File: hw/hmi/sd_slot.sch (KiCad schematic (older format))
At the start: 10 parts, among them J7 SD_Card

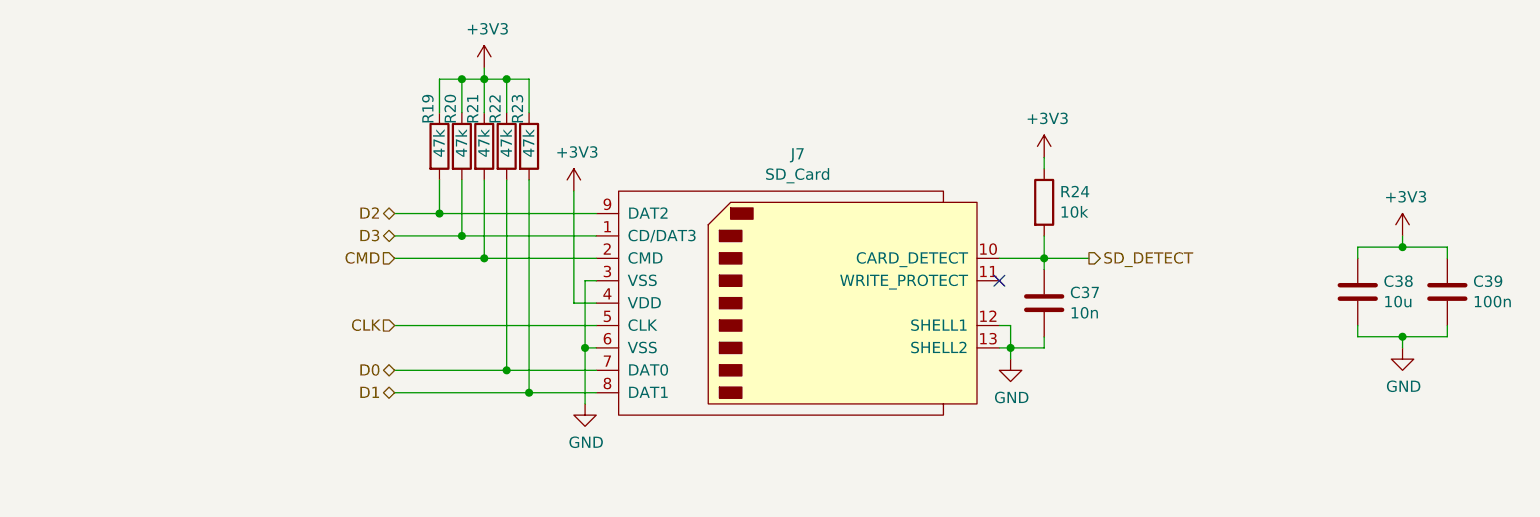
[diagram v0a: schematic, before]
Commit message: Added HMI and SDU boards
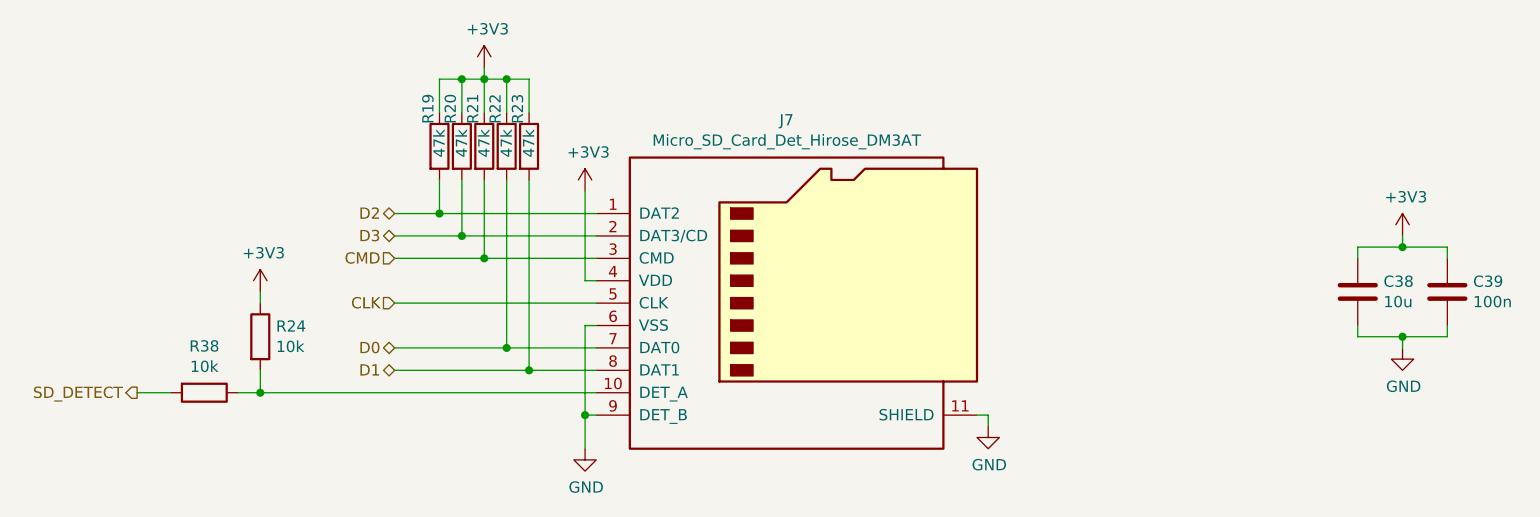
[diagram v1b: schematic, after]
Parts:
- removed C37: 10n, Capacitor_SMD:C_0805_2012Metric, symbol Device:C
- removed J7: SD_Card, Connector_Card:SD_TE_2041021, symbol Connector:SD_Card
- added J7: Micro_SD_Card_Det_Hirose_DM3AT, Connector_Card:microSD_HC_Hirose_DM3AT-SF-PEJM5, symbol Connector:Micro_SD_Card_Det_Hirose_DM3AT
- added R38: 10k, Resistor_SMD:R_0805_2012Metric, symbol Device:R
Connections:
- net +3V3: now also J7.4 (VDD)
- net CLK: now also J7.5 (CLK)
- net CMD: now also J7.3 (CMD)
- net D0: now also J7.7 (DAT0)
- net D1: now also J7.8 (DAT1)
- net D2: now also J7.1 (DAT2)
- net D3: now also J7.2 (DAT3/CD)
- net GND: now also J7.11 (SHIELD), J7.6 (VSS), J7.9 (DET_B)
- net SD_DETECT: now also R38.2; no longer R24.2
- new net: J7.10 (DET_A), R24.2, R38.1
- no-connect marks 1 -> 0
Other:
- moved on the sheet: R24
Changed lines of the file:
@@
 Comment4 ""
 $EndDescr
-$Comp
-L Connector:SD_Card J?
-U 1 1 5C0A7AA3
-P 6400 4000
-AR Path="/5C0A7AA3" Ref="J?"  Part="1"
-AR Path="/5C04B598/5C0A7AA3" Ref="J7"  Part="1"
-F 0 "J7" H 6400 4665 50  0000 C CNN
-F 1 "SD_Card" H 6400 4574 50  0000 C CNN
-F 2 "Connector_Card:SD_TE_2041021" H 6400 4000 50  0001 C CNN
-F 3 "http://portal.fciconnect.com/Comergent//fci/drawing/10067847.pdf" H 6400 4000 50  0001 C CNN
-	1    6400 4000
-	1    0    0    -1
-$EndComp
-Wire Wire Line
-	5500 4300 5100 4300
-Wire Wire Line
-	5500 4400 5200 4400
-Wire Wire Line
-	5500 3900 5450 3900
-Wire Wire Line
-	5450 3900 5450 4200
-Wire Wire Line
-	5450 4200 5500 4200
-Wire Wire Line
-	5450 4200 5450 4450
-Connection ~ 5450 4200
+Wire Wire Line
+	5500 4200 5100 4200
+Wire Wire Line
+	5500 4300 5200 4300
 $Comp
 L power:GND #PWR?
 U 1 1 5C0A7AB1
-P 5450 4450
+P 5450 4650
 AR Path="/5C0A7AB1" Ref="#PWR?"  Part="1"
 AR Path="/5C04B598/5C0A7AB1" Ref="#PWR0172"  Part="1"
-F 0 "#PWR0172" H 5450 4200 50  0001 C CNN
-F 1 "GND" H 5455 4277 50  0000 C CNN
-F 2 "" H 5450 4450 50  0001 C CNN
-F 3 "" H 5450 4450 50  0001 C CNN
-	1    5450 4450
-	1    0    0    -1
-$EndComp
-Wire Wire Line
-	5500 4000 5400 4000
-Wire Wire Line
-	5400 4000 5400 3500
+F 0 "#PWR0172" H 5450 4400 50  0001 C CNN
+F 1 "GND" H 5455 4477 50  0000 C CNN
+F 2 "" H 5450 4650 50  0001 C CNN
+F 3 "" H 5450 4650 50  0001 C CNN
+	1    5450 4650
+	1    0    0    -1
+$EndComp
 $Comp
 L power:+3V3 #PWR?
 U 1 1 5C0A7AB9
-P 5400 3500
+P 5450 3500
 AR Path="/5C0A7AB9" Ref="#PWR?"  Part="1"
 AR Path="/5C04B598/5C0A7AB9" Ref="#PWR0173"  Part="1"
-F 0 "#PWR0173" H 5400 3350 50  0001 C CNN
-F 1 "+3V3" H 5415 3673 50  0000 C CNN
-F 2 "" H 5400 3500 50  0001 C CNN
-F 3 "" H 5400 3500 50  0001 C CNN
-	1    5400 3500
+F 0 "#PWR0173" H 5450 3350 50  0001 C CNN
+F 1 "+3V3" H 5465 3673 50  0000 C CNN
+F 2 "" H 5450 3500 50  0001 C CNN
+F 3 "" H 5450 3500 50  0001 C CNN
+	1    5450 3500
 	1    0    0    -1
 $EndComp
@@
 Wire Wire Line
 	5000 3450 5000 3800
-Wire Wire Line
-	5100 3450 5100 4300
-Wire Wire Line
-	5200 3450 5200 4400
 $Comp
 L power:+3V3 #PWR?
@@
 	5200 3000 5200 3150
 Connection ~ 5100 3000
-Wire Wire Line
-	7300 3800 7500 3800
 $Comp
 L Device:R R?
 U 1 1 5C0A7B0F
-P 7500 3550
+P 4000 4150
 AR Path="/5C0A7B0F" Ref="R?"  Part="1"
 AR Path="/5C04B598/5C0A7B0F" Ref="R24"  Part="1"
-F 0 "R24" H 7570 3596 50  0000 L CNN
-F 1 "10k" H 7570 3505 50  0000 L CNN
-F 2 "Resistor_SMD:R_0805_2012Metric" V 7430 3550 50  0001 C CNN
-F 3 "~" H 7500 3550 50  0001 C CNN
-	1    7500 3550
-	1    0    0    -1
-$EndComp
-Wire Wire Line
-	7500 3700 7500 3800
-Connection ~ 7500 3800
-Wire Wire Line
-	7500 3800 7700 3800
+F 0 "R24" H 4070 4196 50  0000 L CNN
+F 1 "10k" H 4070 4105 50  0000 L CNN
+F 2 "Resistor_SMD:R_0805_2012Metric" V 3930 4150 50  0001 C CNN
+F 3 "~" H 4000 4150 50  0001 C CNN
+	1    4000 4150
+	1    0    0    -1
+$EndComp
 $Comp
 L power:+3V3 #PWR?
 U 1 1 5C0A7B19
-P 7500 3350
+P 4000 3950
 AR Path="/5C0A7B19" Ref="#PWR?"  Part="1"
 AR Path="/5C04B598/5C0A7B19" Ref="#PWR0175"  Part="1"
-F 0 "#PWR0175" H 7500 3200 50  0001 C CNN
-F 1 "+3V3" H 7515 3523 50  0000 C CNN
-F 2 "" H 7500 3350 50  0001 C CNN
-F 3 "" H 7500 3350 50  0001 C CNN
-	1    7500 3350
-	1    0    0    -1
-$EndComp
-Wire Wire Line
-	7500 3350 7500 3400
-$Comp
-L power:GND #PWR?
-U 1 1 5C0A7B21
-P 7350 4250
-AR Path="/5C0A7B21" Ref="#PWR?"  Part="1"
-AR Path="/5C04B598/5C0A7B21" Ref="#PWR0176"  Part="1"
-F 0 "#PWR0176" H 7350 4000 50  0001 C CNN
-F 1 "GND" H 7355 4077 50  0000 C CNN
-F 2 "" H 7350 4250 50  0001 C CNN
-F 3 "" H 7350 4250 50  0001 C CNN
-	1    7350 4250
-	1    0    0    -1
-$EndComp
-Wire Wire Line
-	7350 4250 7350 4200
-Wire Wire Line
-	7350 4100 7300 4100
-Wire Wire Line
-	7300 4200 7350 4200
-Connection ~ 7350 4200
-Wire Wire Line
-	7350 4200 7350 4100
+F 0 "#PWR0175" H 4000 3800 50  0001 C CNN
+F 1 "+3V3" H 4015 4123 50  0000 C CNN
+F 2 "" H 4000 3950 50  0001 C CNN
+F 3 "" H 4000 3950 50  0001 C CNN
+	1    4000 3950
+	1    0    0    -1
+$EndComp
 $Comp
 L Device:C C?
@@
 Wire Wire Line
 	9100 3750 9300 3750
-NoConn ~ 7300 3900
-$Comp
-L Device:C C?
-U 1 1 5C0A7B53
-P 7500 4000
-AR Path="/5C0A7B53" Ref="C?"  Part="1"
-AR Path="/5C04B598/5C0A7B53" Ref="C37"  Part="1"
-F 0 "C37" H 7615 4046 50  0000 L CNN
-F 1 "10n" H 7615 3955 50  0000 L CNN
-F 2 "Capacitor_SMD:C_0805_2012Metric" H 7538 3850 50  0001 C CNN
-F 3 "~" H 7500 4000 50  0001 C CNN
-	1    7500 4000
-	1    0    0    -1
-$EndComp
-Wire Wire Line
-	7500 4150 7500 4200
-Wire Wire Line
-	7500 4200 7350 4200
-Wire Wire Line
-	7500 3850 7500 3800
 Text HLabel 4600 3600 0    50   BiDi ~ 0
 D2
 Text HLabel 4600 3700 0    50   BiDi ~ 0
 D3
+Text HLabel 4600 4200 0    50   BiDi ~ 0
+D0
 Text HLabel 4600 4300 0    50   BiDi ~ 0
-D0
-Text HLabel 4600 4400 0    50   BiDi ~ 0
 D1
-Text HLabel 4600 4100 0    50   Input ~ 0
+Text HLabel 4600 4000 0    50   Input ~ 0
 CLK
 Text HLabel 4600 3800 0    50   Input ~ 0
@@
 Connection ~ 4800 3600
 Wire Wire Line
-	4600 4100 5500 4100
-Wire Wire Line
-	4600 4300 5100 4300
-Connection ~ 5100 4300
-Wire Wire Line
-	4600 4400 5200 4400
-Connection ~ 5200 4400
-Text HLabel 7700 3800 2    50   Output ~ 0
+	4600 4000 5500 4000
+Wire Wire Line
+	4600 4200 5100 4200
+Connection ~ 5100 4200
+Wire Wire Line
+	4600 4300 5200 4300
+Connection ~ 5200 4300
+Text HLabel 3450 4400 0    50   Output ~ 0
 SD_DETECT
+Wire Wire Line
+	5500 4100 5450 4100
+Wire Wire Line
+	5100 3450 5100 4200
+Wire Wire Line
+	5200 3450 5200 4300
+$Comp
+L Connector:Micro_SD_Card_Det_Hirose_DM3AT J7
+U 1 1 5C0CB6F8
+P 6400 4000
+F 0 "J7" H 6350 4817 50  0000 C CNN
+F 1 "Micro_SD_Card_Det_Hirose_DM3AT" H 6350 4726 50  0000 C CNN
+F 2 "Connector_Card:microSD_HC_Hirose_DM3AT-SF-PEJM5" H 8450 4700 50  0001 C CNN
+F 3 "https://www.hirose.com/product/en/download_file/key_name/DM3/category/Catalog/doc_file_id/49662/?file_category_id=4&item_id=195&is_series=1" H 6400 4100 50  0001 C CNN
+	1    6400 4000
+	1    0    0    -1
+$EndComp
+Wire Wire Line
+	5500 4500 5450 4500
+Wire Wire Line
+	5450 4500 5450 4650
+$Comp
+L Device:R R38
+U 1 1 5C0CD5A4
+P 3750 4400
+F 0 "R38" V 3543 4400 50  0000 C CNN
+F 1 "10k" V 3634 4400 50  0000 C CNN
+F 2 "Resistor_SMD:R_0805_2012Metric" V 3680 4400 50  0001 C CNN
+F 3 "~" H 3750 4400 50  0001 C CNN
+	1    3750 4400
+	0    1    1    0
+$EndComp
+Wire Wire Line
+	4000 3950 4000 4000
+Wire Wire Line
+	3450 4400 3600 4400
+Wire Wire Line
+	3900 4400 4000 4400
+Wire Wire Line
+	4000 4400 4000 4300
+Wire Wire Line
+	4000 4400 5500 4400
+Connection ~ 4000 4400
+Connection ~ 5450 4500
+Wire Wire Line
+	5450 4100 5450 4500
+Wire Wire Line
+	5500 3900 5450 3900
+Wire Wire Line
+	5450 3900 5450 3500
+$Comp
+L power:GND #PWR02
+U 1 1 5C0D4611
+P 7250 4550
+F 0 "#PWR02" H 7250 4300 50  0001 C CNN
+F 1 "GND" H 7255 4377 50  0000 C CNN
+F 2 "" H 7250 4550 50  0001 C CNN
+F 3 "" H 7250 4550 50  0001 C CNN
+	1    7250 4550
+	1    0    0    -1
+$EndComp
+Wire Wire Line
+	7250 4550 7250 4500
+Wire Wire Line
+	7250 4500 7200 4500
 $EndSCHEMATC
